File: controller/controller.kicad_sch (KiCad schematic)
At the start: 10 parts, among them SW1 Move Up Btn, SW2 Move Down Btn, SW3 Move Right Btn, SW4 Move Left Btn, SW5 Attack Btn, SW6 Defense Btn, U1 XIAO-RP2040-DIP

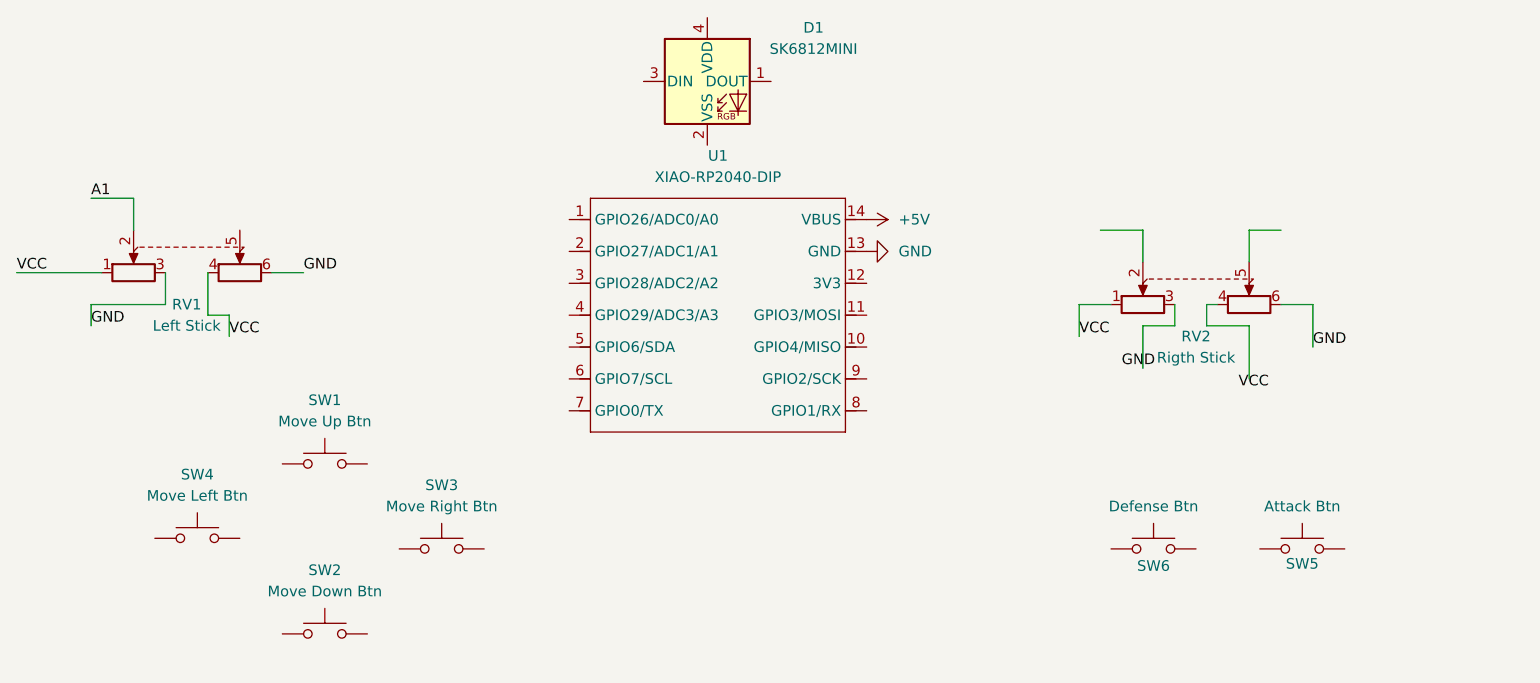
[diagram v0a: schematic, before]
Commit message: So I solved all the errors I was getting in the kicad. Now Schematics are all done. All Which is left is PCB. WHich WIll be done in few hours. I have Changed all the Buttons I used for hackpad to Open Dual PW Push Buttons and I have connected the componenets with each other with the help of labels in the schematic editor. It took a lot of time because this was first time doing alll this because I did not even knew about the labels in the schematic editor.
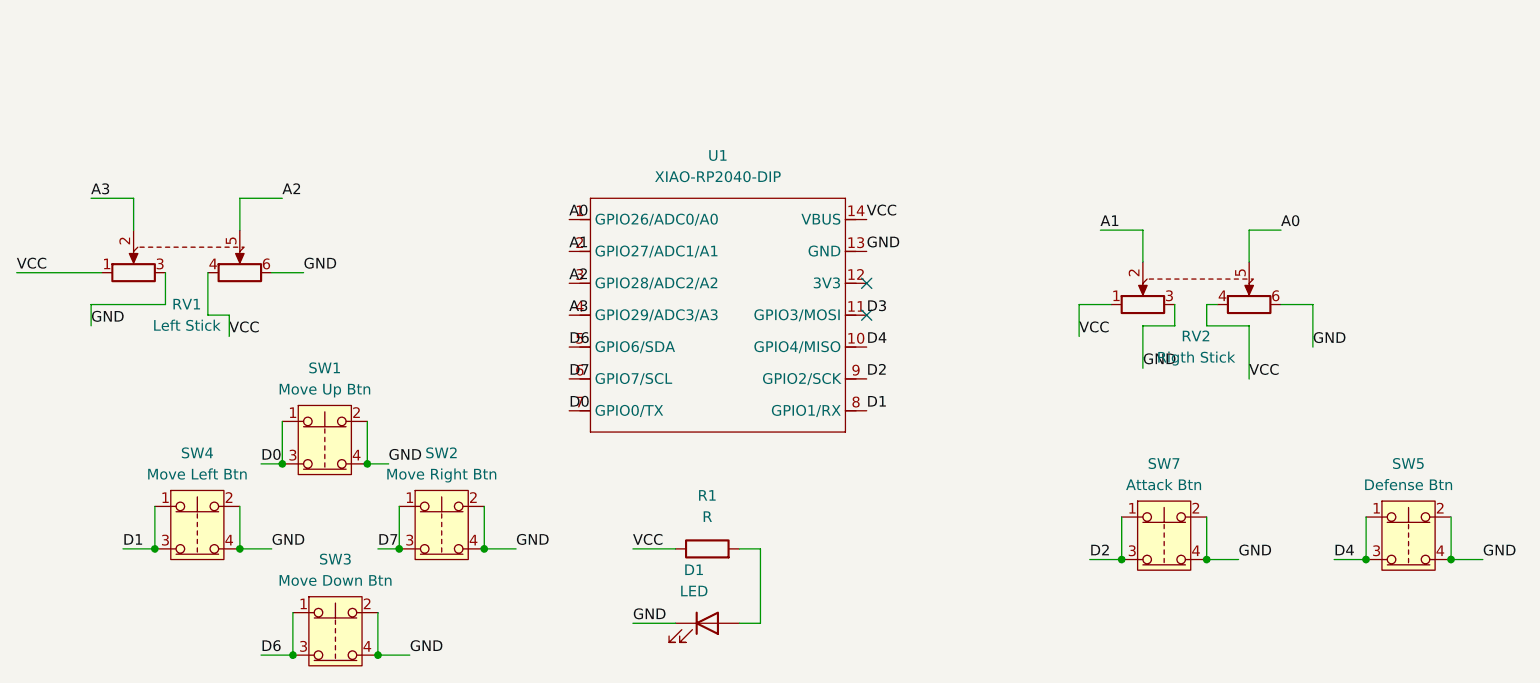
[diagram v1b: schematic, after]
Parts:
- removed D1: SK6812MINI, LED_SMD:LED_SK6812MINI_PLCC4_3.5x3.5mm_P1.75mm, symbol LED:SK6812MINI
- removed SW1: Move Up Btn, Button_Switch_Keyboard:SW_Cherry_MX_1.00u_PCB, symbol Switch:SW_Push
- removed SW2: Move Down Btn, Button_Switch_Keyboard:SW_Cherry_MX_1.00u_PCB, symbol Switch:SW_Push
- removed SW3: Move Right Btn, Button_Switch_Keyboard:SW_Cherry_MX_1.00u_PCB, symbol Switch:SW_Push
- removed SW4: Move Left Btn, Button_Switch_Keyboard:SW_Cherry_MX_1.00u_PCB, symbol Switch:SW_Push
- removed SW5: Attack Btn, Button_Switch_Keyboard:SW_Cherry_MX_1.00u_PCB, symbol Switch:SW_Push
- removed SW6: Defense Btn, Button_Switch_Keyboard:SW_Cherry_MX_1.00u_PCB, symbol Switch:SW_Push
- added D1: LED, symbol Device:LED
- added R1: R, symbol Device:R
- added SW1: Move Up Btn, symbol Switch:SW_Push_Open_Dual
- added SW2: Move Right Btn, symbol Switch:SW_Push_Open_Dual
- added SW3: Move Down Btn, symbol Switch:SW_Push_Open_Dual
- added SW4: Move Left Btn, symbol Switch:SW_Push_Open_Dual
- added SW5: Defense Btn, symbol Switch:SW_Push_Open_Dual
- added SW7: Attack Btn, symbol Switch:SW_Push_Open_Dual
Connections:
- net +5V is gone; now on net VCC: U1.14 (VBUS)
- net A1: now also RV2.2, U1.2 (GPIO27/ADC1/A1); no longer RV1.2
- net GND: now also RV2.3, D1.1 (K), SW1.2, SW1.4, SW2.2, SW2.4, SW3.2, SW3.4, SW4.2, SW4.4, SW5.2, SW5.4, SW7.2, SW7.4
- net VCC: now also RV2.4, R1.1
- net A0: now reaches RV2.5
- net A0: now also U1.1 (GPIO26/ADC0/A0)
- net A2: now reaches RV1.5
- net A2: now also U1.3 (GPIO28/ADC2/A2)
- net D4: now reaches U1.10 (GPIO4/MISO)
- net D4: now also SW5.1, SW5.3
- net D3: now reaches U1.11 (GPIO3/MOSI)
- net A3: now reaches U1.4 (GPIO29/ADC3/A3)
- net A3: now also RV1.2
- net D6: now reaches U1.5 (GPIO6/SDA)
- net D6: now also SW3.1, SW3.3
- net D7: now reaches U1.6 (GPIO7/SCL)
- net D7: now also SW2.1, SW2.3
- net D0: now reaches U1.7 (GPIO0/TX)
- net D0: now also SW1.1, SW1.3
- net D1: now reaches U1.8 (GPIO1/RX)
- net D1: now also SW4.1, SW4.3
- net D2: now reaches U1.9 (GPIO2/SCK)
- net D2: now also SW7.1, SW7.3
- new net: D1.2 (A), R1.2
- no-connect marks 0 -> 2

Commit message: SO I have Started and finsihed the PCb. I had to assign all the footprint to all the components in the schematic editor. Then After Importing them I had to import a Graphic Picture of Controller Outline. SO I put all the componenets in the controller outline. Then I started all the componenets with each other (Although I forgot to reimport the microcontroller because it did not had labels). I have Connected all the Data Pins and Vcc Pins on the front (with one exception) and all the Ground Pins on the Back SIde. I Have Connected the LED with the resistor and then second end with Ground. The Resistor is Directy COnnected with the VCC. Now I am Only facing One Problem which is that there is a small gap in my controller outline because of which the kicad is not abe to properly cut the pcb into my desired shape.
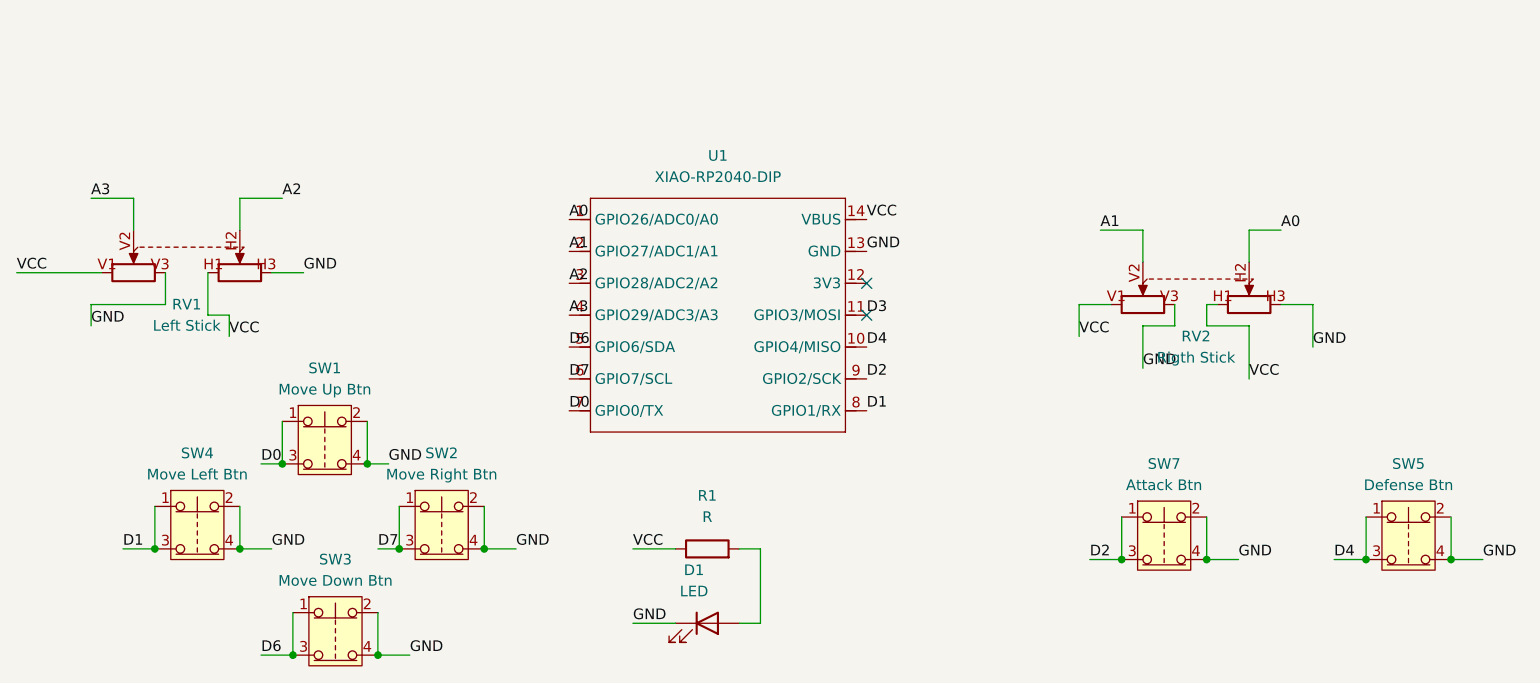
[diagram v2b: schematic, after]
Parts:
- D1: footprint (none) -> LED_THT:LED_D5.0mm
- R1: footprint (none) -> Resistor_THT:R_Axial_DIN0207_L6.3mm_D2.5mm_P10.16mm_Horizontal
- RV1, RV2: footprint (none) -> Joystick:XDCR_COM-09032
- SW1, SW2, SW3, SW4, SW5, SW7: footprint (none) -> Button_Switch_THT:Push_E-Switch_KS01Q01
- U1: footprint Module:MOUDLE14P-XIAO-DIP-SMD -> OPL_Kicad:XIAO-RP2040-DIP
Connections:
- net A0: now also RV2.H2 (5); no longer RV2.5
- net A1: now also RV2.V2 (2); no longer RV2.2
- net A2: now also RV1.H2 (5); no longer RV1.5
- net A3: now also RV1.V2 (2); no longer RV1.2
- net GND: now also RV1.H3 (6), RV1.V3 (3), RV2.H3 (6), RV2.V3 (3); no longer RV1.3, RV1.6, RV2.3, RV2.6
- net VCC: now also RV1.H1 (4), RV1.V1 (1), RV2.H1 (4), RV2.V1 (1); no longer RV1.1, RV1.4, RV2.1, RV2.4
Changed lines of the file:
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@@
 			)
 		)
-		(property "Footprint" ""
+		(property "Footprint" "Joystick:XDCR_COM-09032"
 			(at 220.98 59.055 0)
 			(effects
@@
 			)
 		)
-		(pin "6"
-		)
-		(pin "3"
-		)
-		(pin "2"
-		)
-		(pin "1"
-		)
-		(pin "4"
-		)
-		(pin "5"
+		(pin "V3"
+		)
+		(pin "V2"
+		)
+		(pin "H2"
+		)
+		(pin "H1"
+		)
+		(pin "V1"
+		)
+		(pin "H3"
 		)
 		(instances
@@
 			)
 		)
-		(property "Footprint" ""
+		(property "Footprint" "Button_Switch_THT:Push_E-Switch_KS01Q01"
 			(at 111.76 91.44 0)
 			(effects
@@
 			)
 		)
-		(property "Footprint" ""
+		(property "Footprint" "LED_THT:LED_D5.0mm"
 			(at 156.21 97.79 0)
 			(effects
@@
 			)
 		)
-		(property "Footprint" ""
+		(property "Footprint" "Button_Switch_THT:Push_E-Switch_KS01Q01"
 			(at 110.49 68.58 0)
 			(effects
@@
 			)
 		)
-		(property "Footprint" ""
+		(property "Footprint" "Button_Switch_THT:Push_E-Switch_KS01Q01"
 			(at 240.03 80.01 0)
 			(effects
@@
 			)
 		)
-		(property "Footprint" ""
+		(property "Footprint" "Button_Switch_THT:Push_E-Switch_KS01Q01"
 			(at 210.82 80.01 0)
 			(effects
@@
 	)
 	(symbol
+		(lib_name "R_Potentiometer_Dual_1")
 		(lib_id "Device:R_Potentiometer_Dual")
 		(at 93.98 53.34 0)
@@
 			)
 		)
-		(property "Footprint" ""
+		(property "Footprint" "Joystick:XDCR_COM-09032"
+			(at 100.076 53.34 0)
+			(effects
+				(font
+					(size 1.27 1.27)
+				)
+				(hide yes)
+			)
+		)
+		(property "Datasheet" "~"
 			(at 100.33 55.245 0)
 			(effects
@@
 			)
 		)
-		(property "Datasheet" "~"
-			(at 100.33 55.245 0)
-			(effects
-				(font
-					(size 1.27 1.27)
-				)
-				(hide yes)
-			)
-		)
 		(property "Description" "Dual potentiometer"
-			(at 93.98 53.34 0)
-			(effects
-				(font
-					(size 1.27 1.27)
-				)
-				(hide yes)
-			)
-		)
-		(pin "6"
-		)
-		(pin "3"
-		)
-		(pin "2"
-		)
-		(pin "1"
-		)
-		(pin "4"
-		)
-		(pin "5"
+			(at 93.98 52.07 0)
+			(effects
+				(font
+					(size 1.27 1.27)
+				)
+				(hide yes)
+			)
+		)
+		(pin "V1"
+		)
+		(pin "V2"
+		)
+		(pin "V3"
+		)
+		(pin "H2"
+		)
+		(pin "H1"
+		)
+		(pin "H3"
 		)
 		(instances
@@
 			)
 		)
-		(property "Footprint" "Module:MOUDLE14P-XIAO-DIP-SMD"
+		(property "Footprint" "OPL_Kicad:XIAO-RP2040-DIP"
 			(at 157.988 76.708 0)
 			(effects
@@
 			)
 		)
-		(property "Footprint" ""
+		(property "Footprint" "Button_Switch_THT:Push_E-Switch_KS01Q01"
 			(at 95.25 78.74 0)
 			(effects
@@
 			)
 		)
-		(property "Footprint" ""
+		(property "Footprint" "Button_Switch_THT:Push_E-Switch_KS01Q01"
 			(at 124.46 78.74 0)
 			(effects
@@
 			)
 		)
-		(property "Footprint" ""
+		(property "Footprint" "Resistor_THT:R_Axial_DIN0207_L6.3mm_D2.5mm_P10.16mm_Horizontal"
 			(at 156.21 90.678 90)
 			(effects
